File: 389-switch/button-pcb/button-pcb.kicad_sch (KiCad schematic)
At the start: 6 parts, among them J1 Conn_01x04, SW1 SW_DIP_x01

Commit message: changing pcb and creating gerber files
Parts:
- R1, R2: footprint Resistor_THT:R_Axial_DIN0207_L6.3mm_D2.5mm_P7.62mm_Horizontal -> Resistor_THT:R_Axial_DIN0207_L6.3mm_D2.5mm_P2.54mm_Vertical

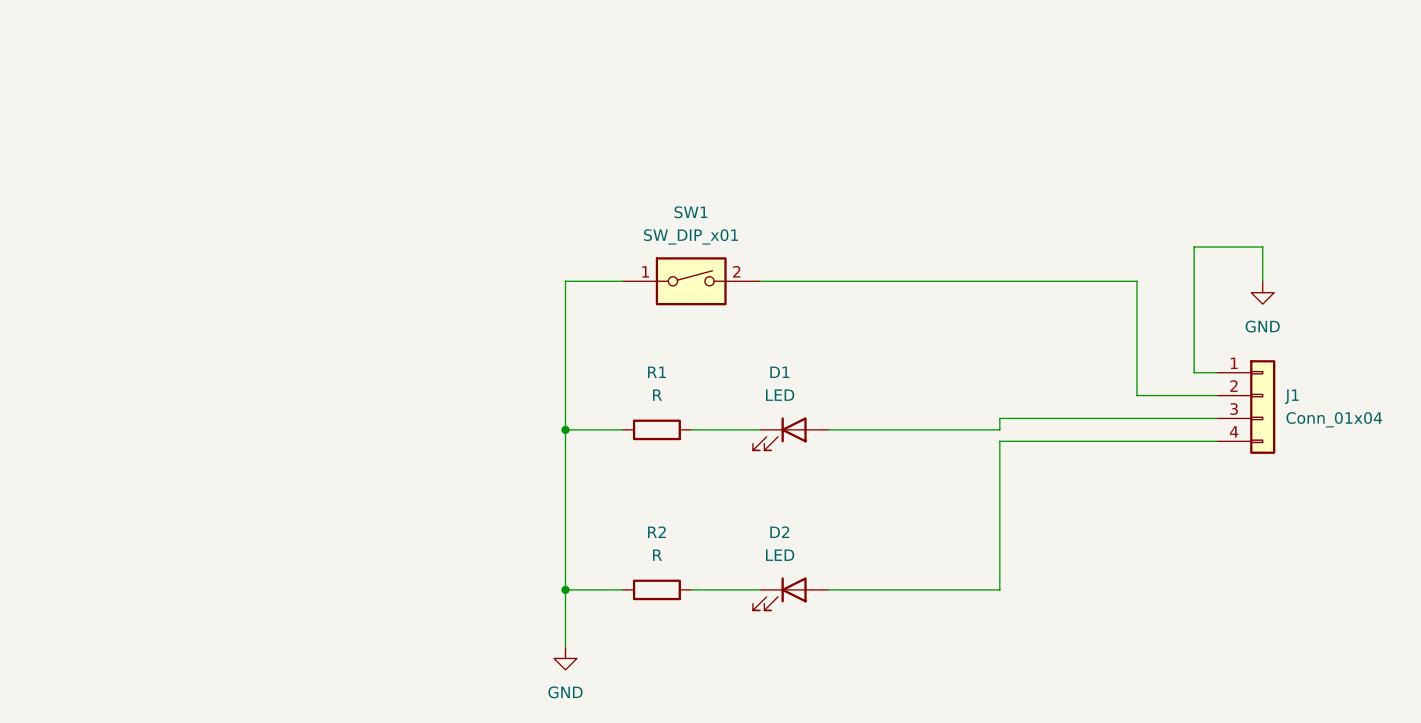
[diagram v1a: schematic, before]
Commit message: adding controller board pcb
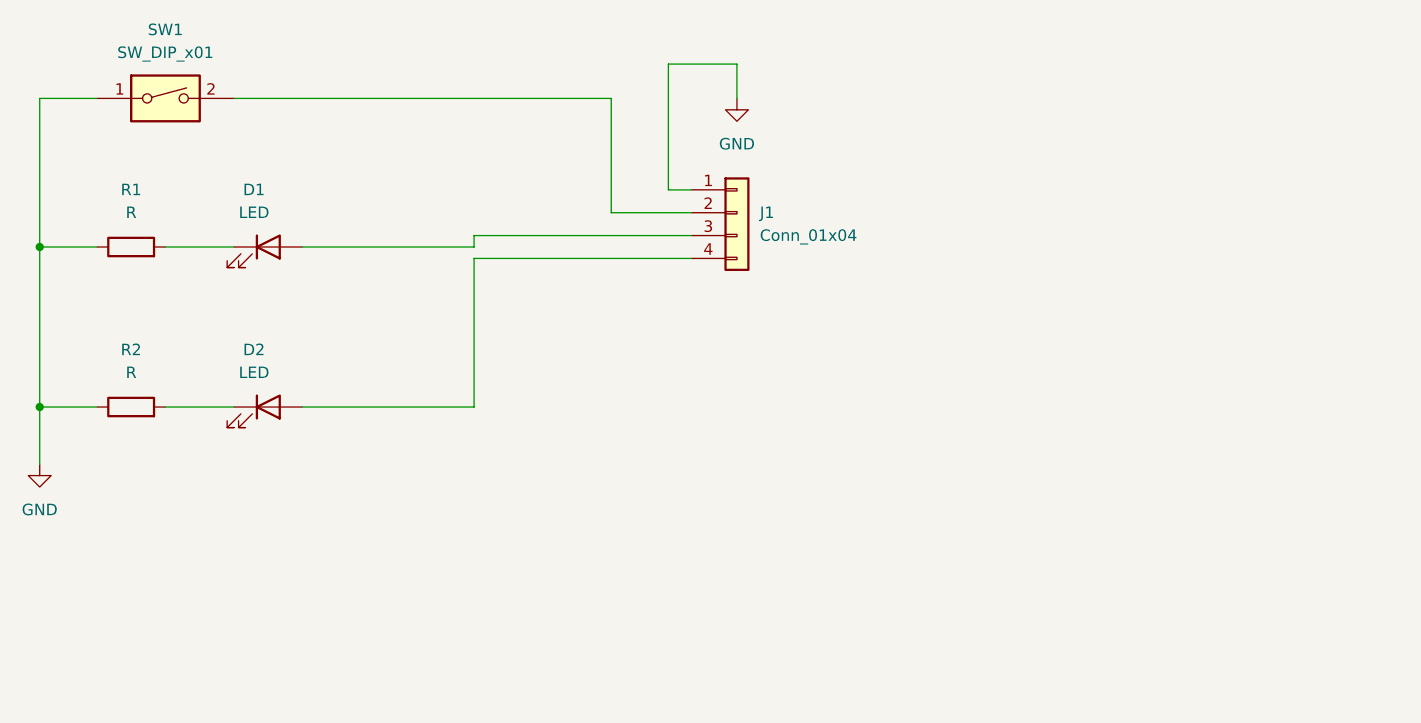
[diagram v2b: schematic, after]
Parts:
- J1: footprint samuel:ZH-1.5mm-4p -> Connector_JST:JST_ZH_B4B-ZR_1x04_P1.50mm_Vertical
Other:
- moved on the sheet: D1, D2, J1, R1, R2, SW1

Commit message: preparing for Production
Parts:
- R1, R2: footprint Resistor_THT:R_Axial_DIN0207_L6.3mm_D2.5mm_P2.54mm_Vertical -> Resistor_SMD:R_1206_3216Metric_Pad1.30x1.75mm_HandSolder
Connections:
- net GND: now also J1.4 (Pin_4); no longer J1.1 (Pin_1)
- net at D2.2 (A): now also J1.3 (Pin_3); no longer J1.4 (Pin_4)
- net at D1.2 (A): now also J1.2 (Pin_2); no longer J1.3 (Pin_3)
- net at SW1.2: now also J1.1 (Pin_1); no longer J1.2 (Pin_2)
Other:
- moved on the sheet: J1
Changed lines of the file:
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@@
+	(wire
+		(pts
+			(xy 128.27 69.85) (xy 128.27 64.77)
+		)
+		(stroke
+			(width 0)
+			(type default)
+		)
+	)
+	(wire
+		(pts
+			(xy 128.27 64.77) (xy 132.08 64.77)
+		)
+		(stroke
+			(width 0)
+			(type default)
+		)
+	)
 	(wire
 		(pts
@@
 	(wire
 		(pts
-			(xy 104.14 59.69) (xy 128.27 59.69)
-		)
-		(stroke
-			(width 0)
-			(type default)
-		)
-	)
-	(wire
-		(pts
 			(xy 85.09 60.96) (xy 104.14 60.96)
 		)
@@
 	(wire
 		(pts
-			(xy 125.73 40.64) (xy 133.35 40.64)
-		)
-		(stroke
-			(width 0)
-			(type default)
-		)
-	)
-	(wire
-		(pts
 			(xy 55.88 78.74) (xy 55.88 85.09)
 		)
@@
 	(wire
 		(pts
-			(xy 128.27 57.15) (xy 119.38 57.15)
-		)
-		(stroke
-			(width 0)
-			(type default)
-		)
-	)
-	(wire
-		(pts
-			(xy 128.27 54.61) (xy 125.73 54.61)
+			(xy 119.38 57.15) (xy 132.08 57.15)
+		)
+		(stroke
+			(width 0)
+			(type default)
+		)
+	)
+	(wire
+		(pts
+			(xy 104.14 59.69) (xy 132.08 59.69)
+		)
+		(stroke
+			(width 0)
+			(type default)
+		)
+	)
+	(wire
+		(pts
+			(xy 104.14 62.23) (xy 132.08 62.23)
 		)
 		(stroke
@@
 	(wire
 		(pts
-			(xy 128.27 62.23) (xy 104.14 62.23)
-		)
-		(stroke
-			(width 0)
-			(type default)
-		)
-	)
-	(wire
-		(pts
 			(xy 104.14 62.23) (xy 104.14 78.74)
 		)
@@
 		)
 	)
-	(wire
-		(pts
-			(xy 125.73 54.61) (xy 125.73 40.64)
-		)
-		(stroke
-			(width 0)
-			(type default)
-		)
-	)
-	(wire
-		(pts
-			(xy 133.35 40.64) (xy 133.35 44.45)
-		)
-		(stroke
-			(width 0)
-			(type default)
-		)
-	)
 	(symbol
 		(lib_id "power:GND")
-		(at 133.35 44.45 0)
+		(at 128.27 69.85 0)
 		(unit 1)
 		(exclude_from_sim no)
@@
 		(fields_autoplaced yes)
 		(property "Reference" "#PWR0101"
-			(at 133.35 50.8 0)
+			(at 128.27 76.2 0)
 			(effects
 				(font
@@
 		)
 		(property "Value" "GND"
-			(at 133.35 49.53 0)
+			(at 128.27 74.93 0)
 			(effects
 				(font
@@
 		)
 		(property "Footprint" ""
-			(at 133.35 44.45 0)
+			(at 128.27 69.85 0)
 			(effects
 				(font
@@
 		)
 		(property "Datasheet" ""
-			(at 133.35 44.45 0)
-			(effects
-				(font
-					(size 1.27 1.27)
-				)
-				(hide yes)
-			)
-		)
-		(property "Description" ""
-			(at 133.35 44.45 0)
+			(at 128.27 69.85 0)
+			(effects
+				(font
+					(size 1.27 1.27)
+				)
+				(hide yes)
+			)
+		)
+		(property "Description" ""
+			(at 128.27 69.85 0)
 			(effects
 				(font
@@
 			)
 		)
-		(property "Footprint" "Resistor_THT:R_Axial_DIN0207_L6.3mm_D2.5mm_P2.54mm_Vertical"
+		(property "Footprint" "Resistor_SMD:R_1206_3216Metric_Pad1.30x1.75mm_HandSolder"
 			(at 66.04 80.518 90)
 			(effects
@@
 			)
 		)
-		(property "Footprint" "Resistor_THT:R_Axial_DIN0207_L6.3mm_D2.5mm_P2.54mm_Vertical"
+		(property "Footprint" "Resistor_SMD:R_1206_3216Metric_Pad1.30x1.75mm_HandSolder"
 			(at 66.04 62.738 90)
 			(effects
@@
 	(symbol
 		(lib_id "Connector_Generic:Conn_01x04")
-		(at 133.35 57.15 0)
+		(at 137.16 59.69 0)
 		(unit 1)
 		(exclude_from_sim no)
@@
 		(fields_autoplaced yes)
 		(property "Reference" "J1"
-			(at 135.89 57.1499 0)
+			(at 139.7 59.6899 0)
 			(effects
 				(font
@@
 		)
 		(property "Value" "Conn_01x04"
-			(at 135.89 59.6899 0)
+			(at 139.7 62.2299 0)
 			(effects
 				(font
@@
 		)
 		(property "Footprint" "Connector_JST:JST_ZH_B4B-ZR_1x04_P1.50mm_Vertical"
-			(at 133.35 57.15 0)
+			(at 137.16 59.69 0)
 			(effects
 				(font
@@
 		)
 		(property "Datasheet" "~"
-			(at 133.35 57.15 0)
-			(effects
-				(font
-					(size 1.27 1.27)
-				)
-				(hide yes)
-			)
-		)
-		(property "Description" ""
-			(at 133.35 57.15 0)
-			(effects
-				(font
+			(at 137.16 59.69 0)
+			(effects
+				(font
+					(size 1.27 1.27)
+				)
+				(hide yes)
+			)
+		)
+		(property "Description" ""
+			(at 137.16 59.69 0)
+			(effects
+				(font
